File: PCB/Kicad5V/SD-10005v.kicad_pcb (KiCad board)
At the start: 2 copper layers, 72 x 82.2 mm, 6 parts, among them CON1 SC3000-Edge, J1 Conn_01x20, J2 Conn_01x20, SW1 SW_Push

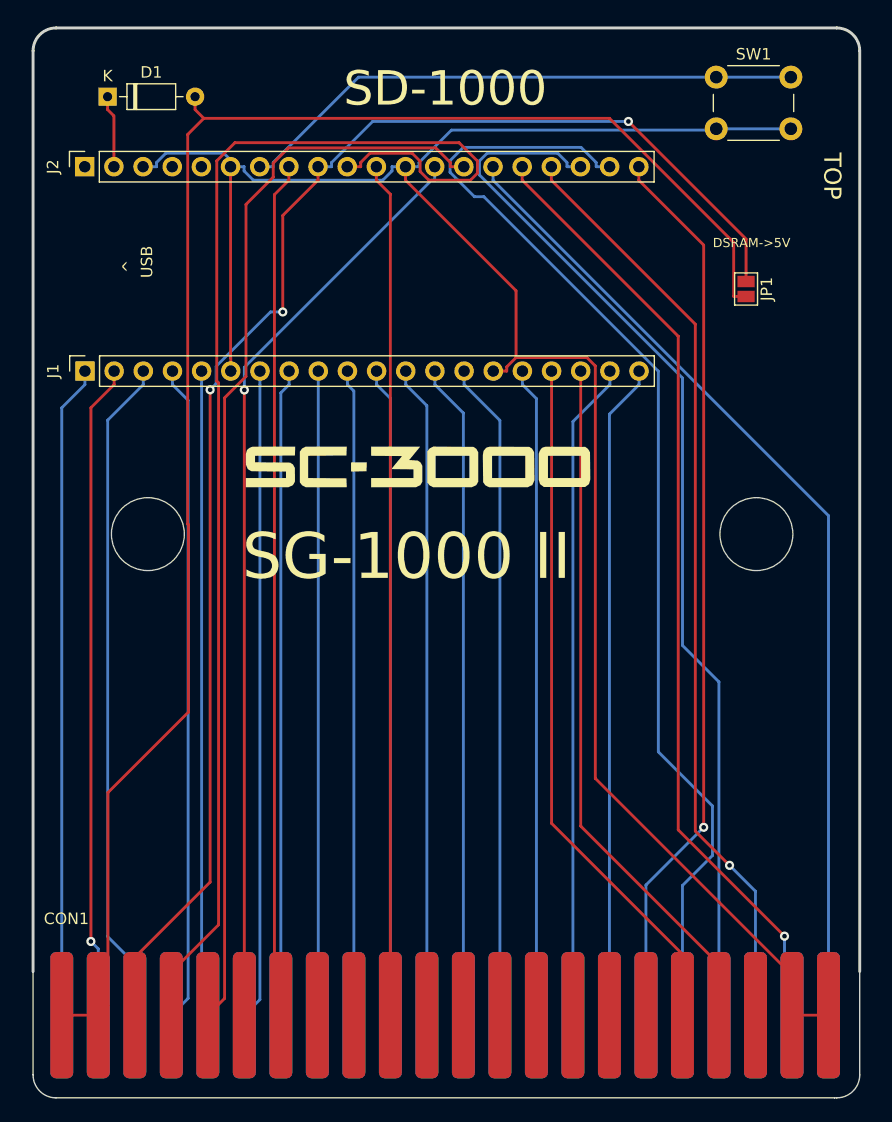
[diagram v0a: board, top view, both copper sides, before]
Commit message: Update PCB
-- Ground plane added to TOP & BOTTOM layer
-- Better routing for some tracks
-- Production files updated
-- JLCPCB DRU file added
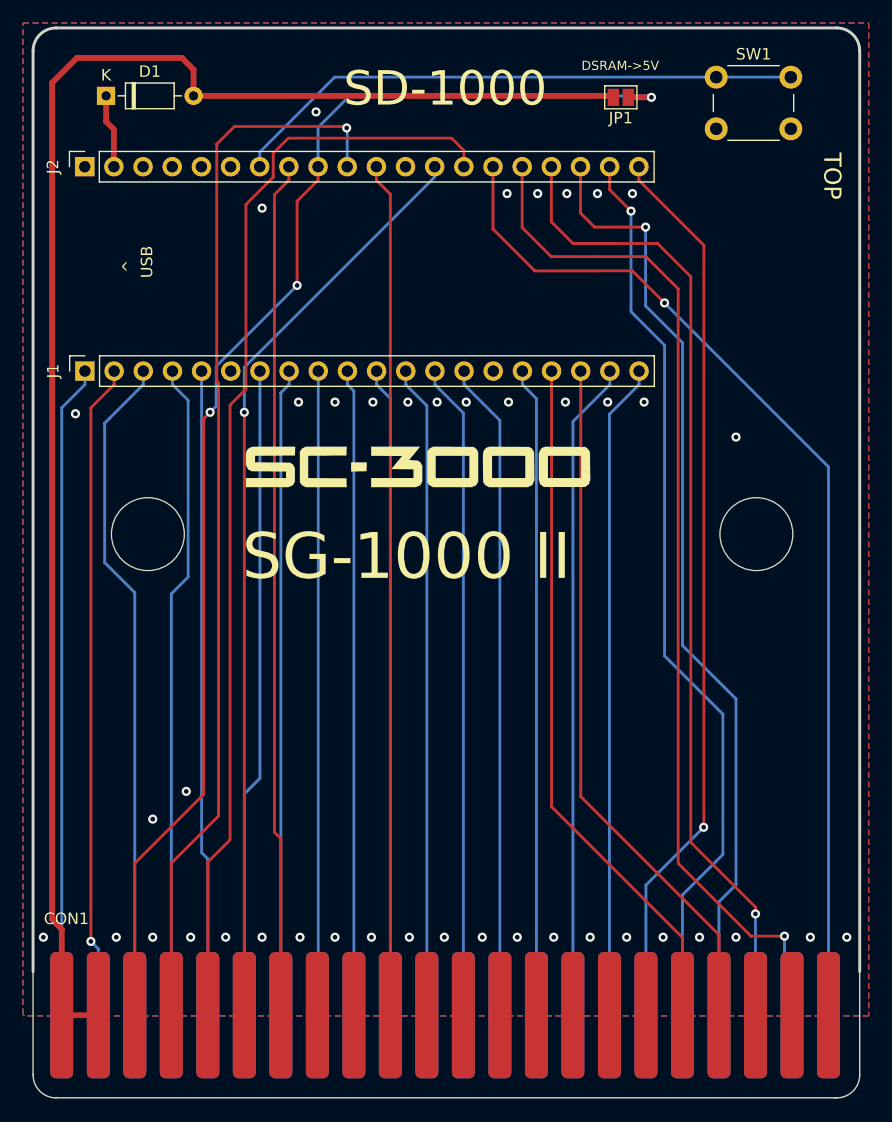
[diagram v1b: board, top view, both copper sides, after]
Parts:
- D1: value Diode -> Diode
- moved JP1 19.9 mm to (123.2, 37.0), turned to 180 degrees
- moved D1 0.15 mm to (78.4, 36.8)
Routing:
- net GND: track 176.3 -> 0.00 mm, vias 0 -> 42
- net ~{CEROM2}: track 115.1 -> 93.0 mm, vias 0 -> 1
- net D3: track 100.8 -> 79.4 mm, vias 0 -> 1
- net ~{DSRAM}: track 128.2 -> 116.2 mm
- net D4: track 92.8 -> 82.7 mm, vias 0 -> 1
- net D6: track 83.6 -> 90.2 mm
- net +5V: track 143.8 -> 137.4 mm
- net D7: track 86.0 -> 91.0 mm, vias 0 -> 1
- net D5: track 81.3 -> 85.6 mm
- net ~{MEMR}: track 94.6 -> 96.4 mm
- net RST: track 49.7 -> 50.2 mm
- added copper zone on B.Cu, net GND
- added copper zone on F.Cu, net GND
